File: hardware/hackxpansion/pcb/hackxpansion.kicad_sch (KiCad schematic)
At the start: 0 parts

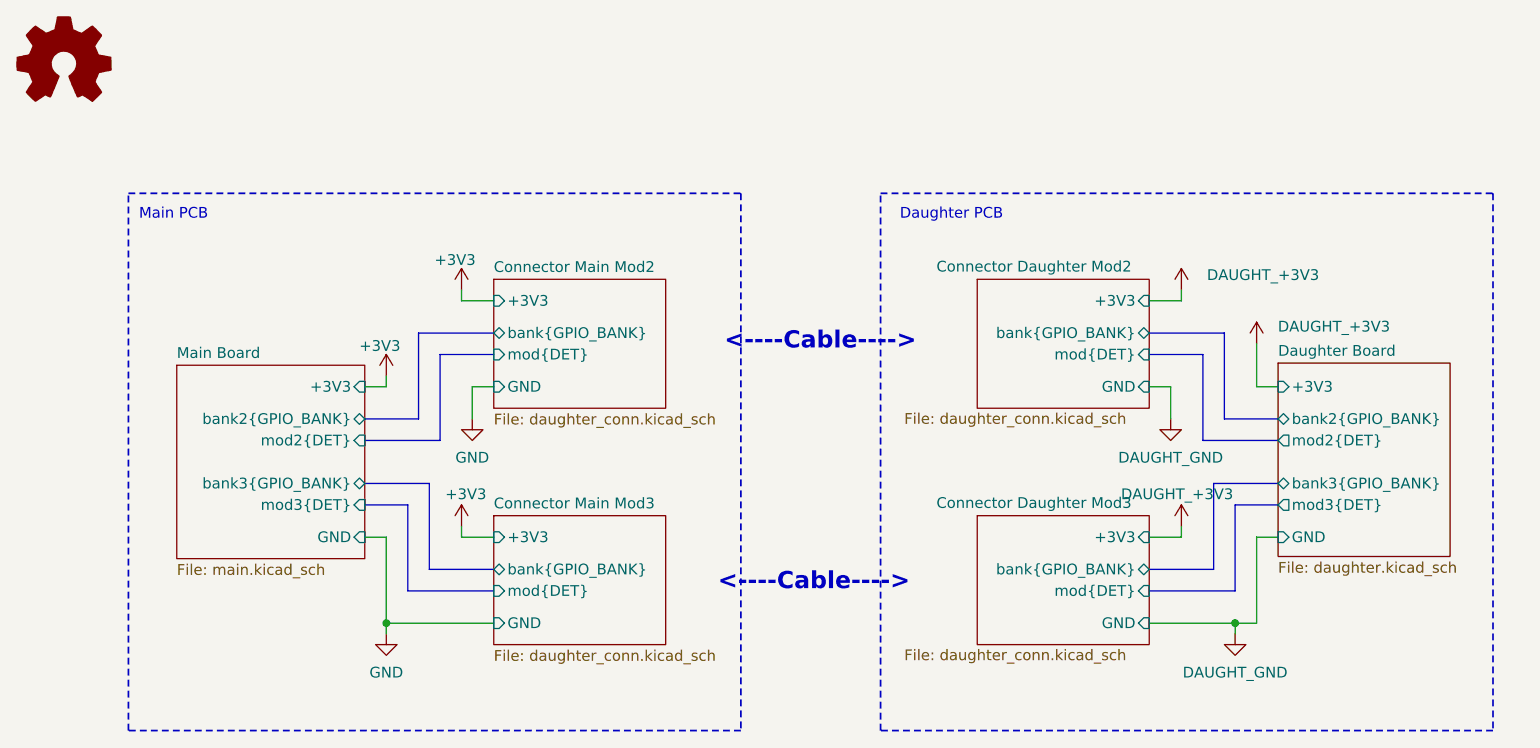
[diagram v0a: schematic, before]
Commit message: started moving resistors from daughter to main board
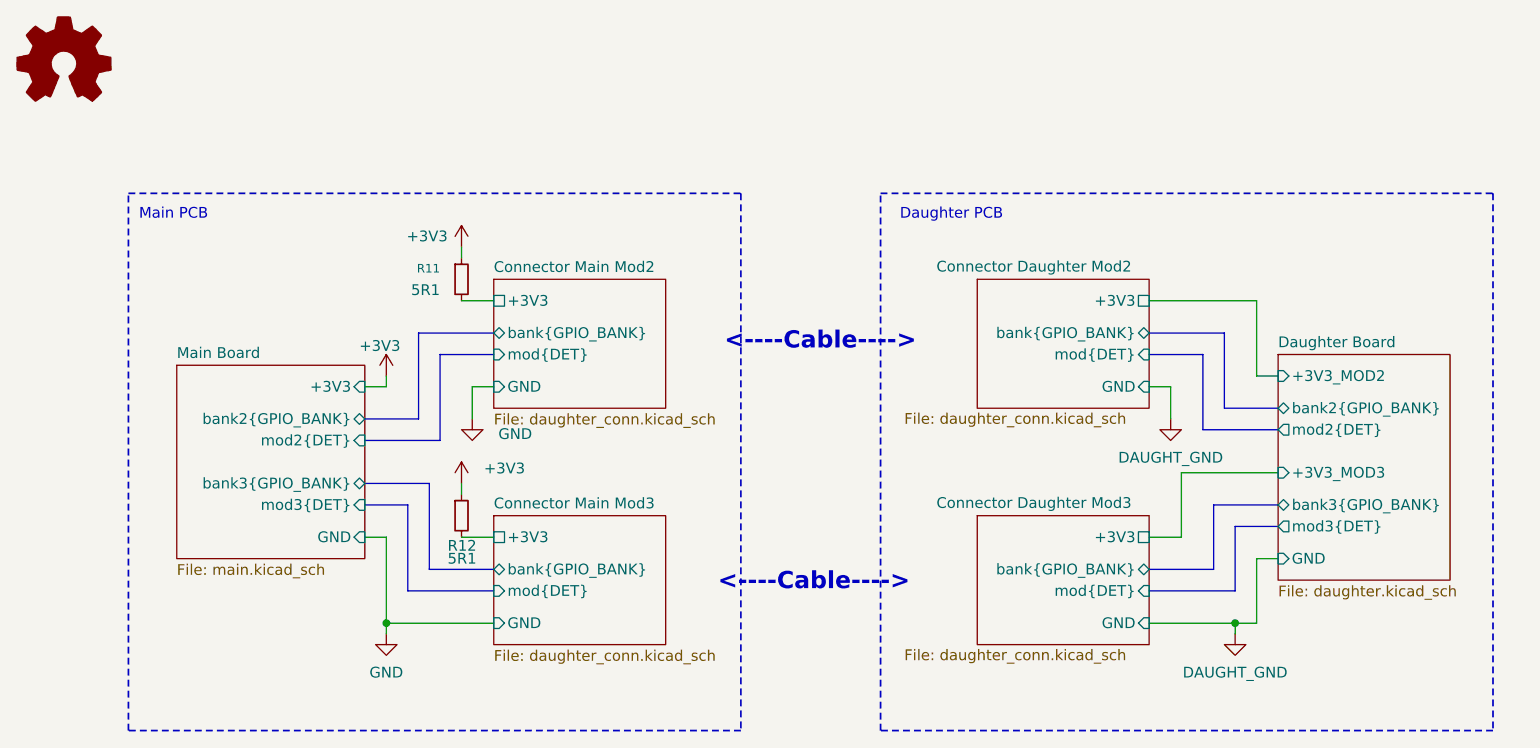
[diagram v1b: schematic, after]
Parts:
- added R11, R12: 5R1, Resistor_SMD:R_0402_1005Metric, symbol Device:R_Small
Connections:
- net +3V3: now also R11.1, R12.1
- new net Connector Main Mod2/+3V3: R11.2
- new net Connector Main Mod3/+3V3: R12.2
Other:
- sheet Daughter Board ports: added +3V3_MOD2, +3V3_MOD3; removed +3V3

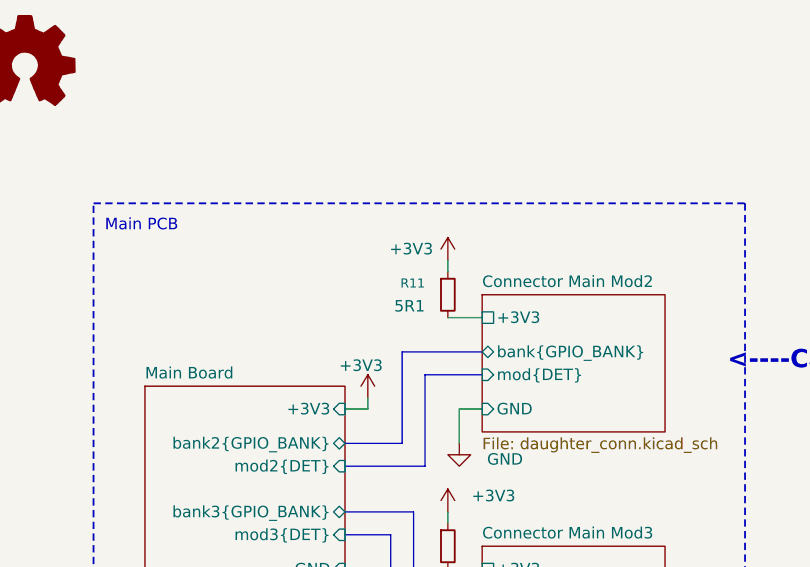
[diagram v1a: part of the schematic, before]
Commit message: replaced battery connector with test pads
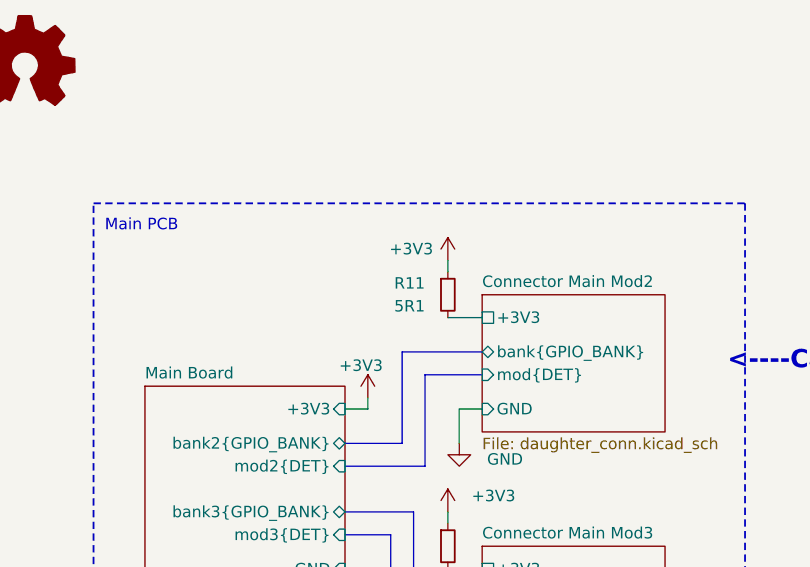
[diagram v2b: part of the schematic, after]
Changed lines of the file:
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@@
 			(effects
 				(font
-					(size 1.016 1.016)
+					(size 1.27 1.27)
 				)
 				(justify right)
